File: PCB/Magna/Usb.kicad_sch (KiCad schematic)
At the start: 30 parts, among them J801 USB_A, J802 USB_C_Receptacle_USB2.0, J803 USB_B, U801 USBLC6-4SC6, U802 USB3300-EZK

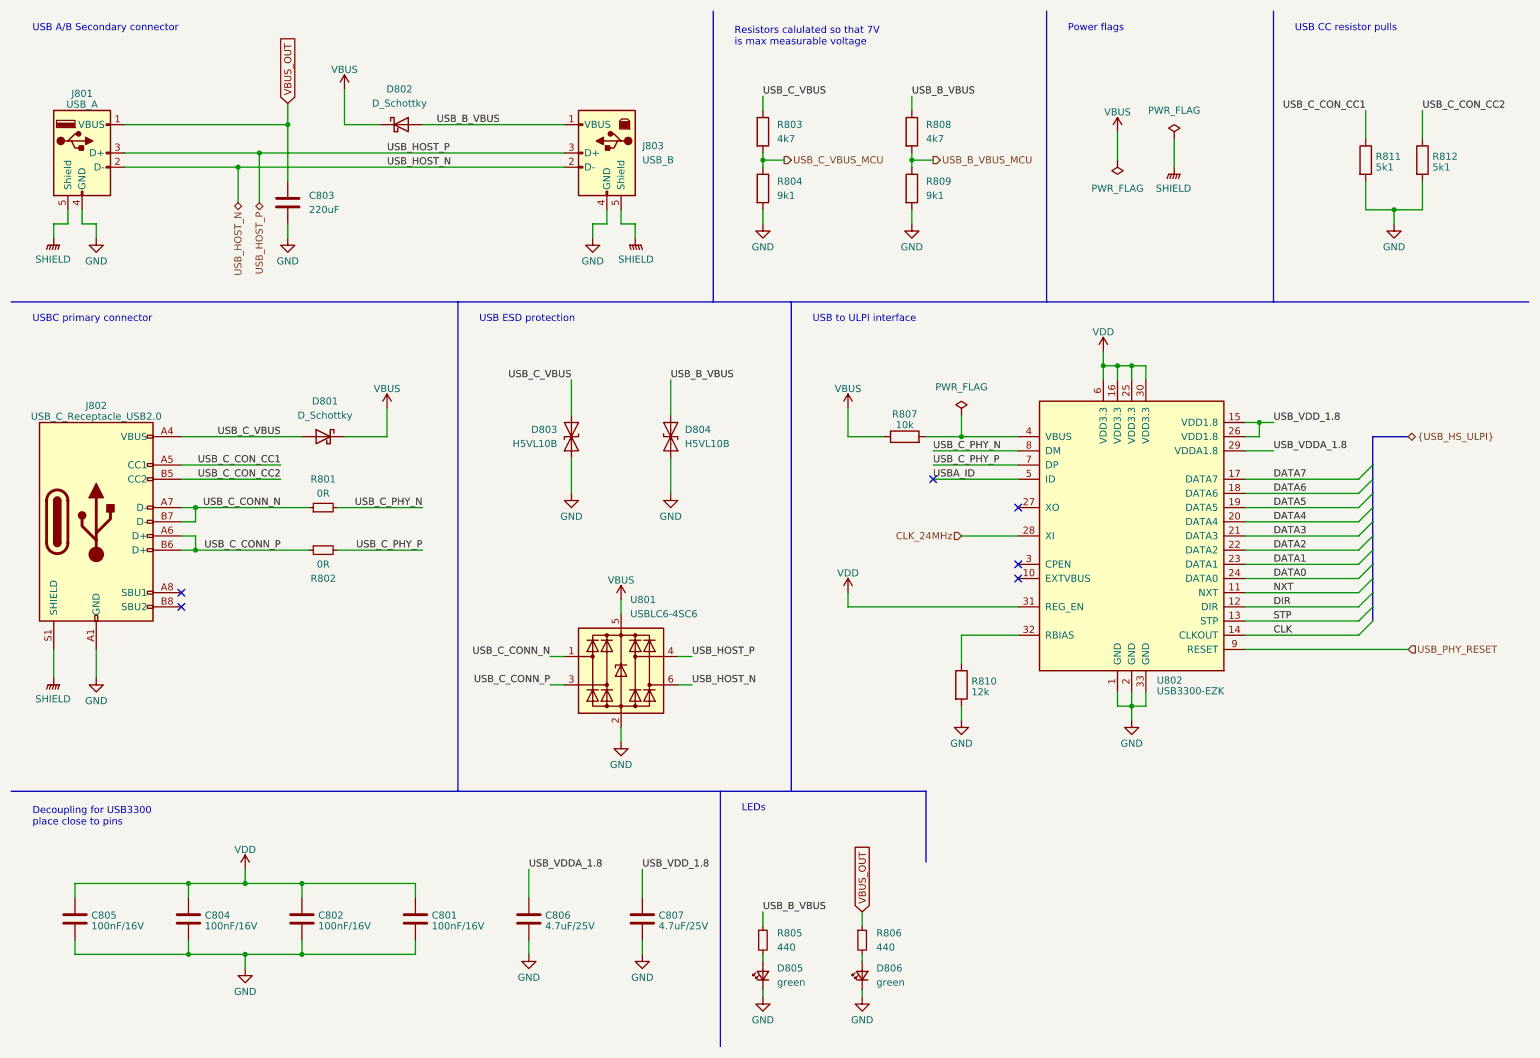
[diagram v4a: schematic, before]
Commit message: Select parts for all components
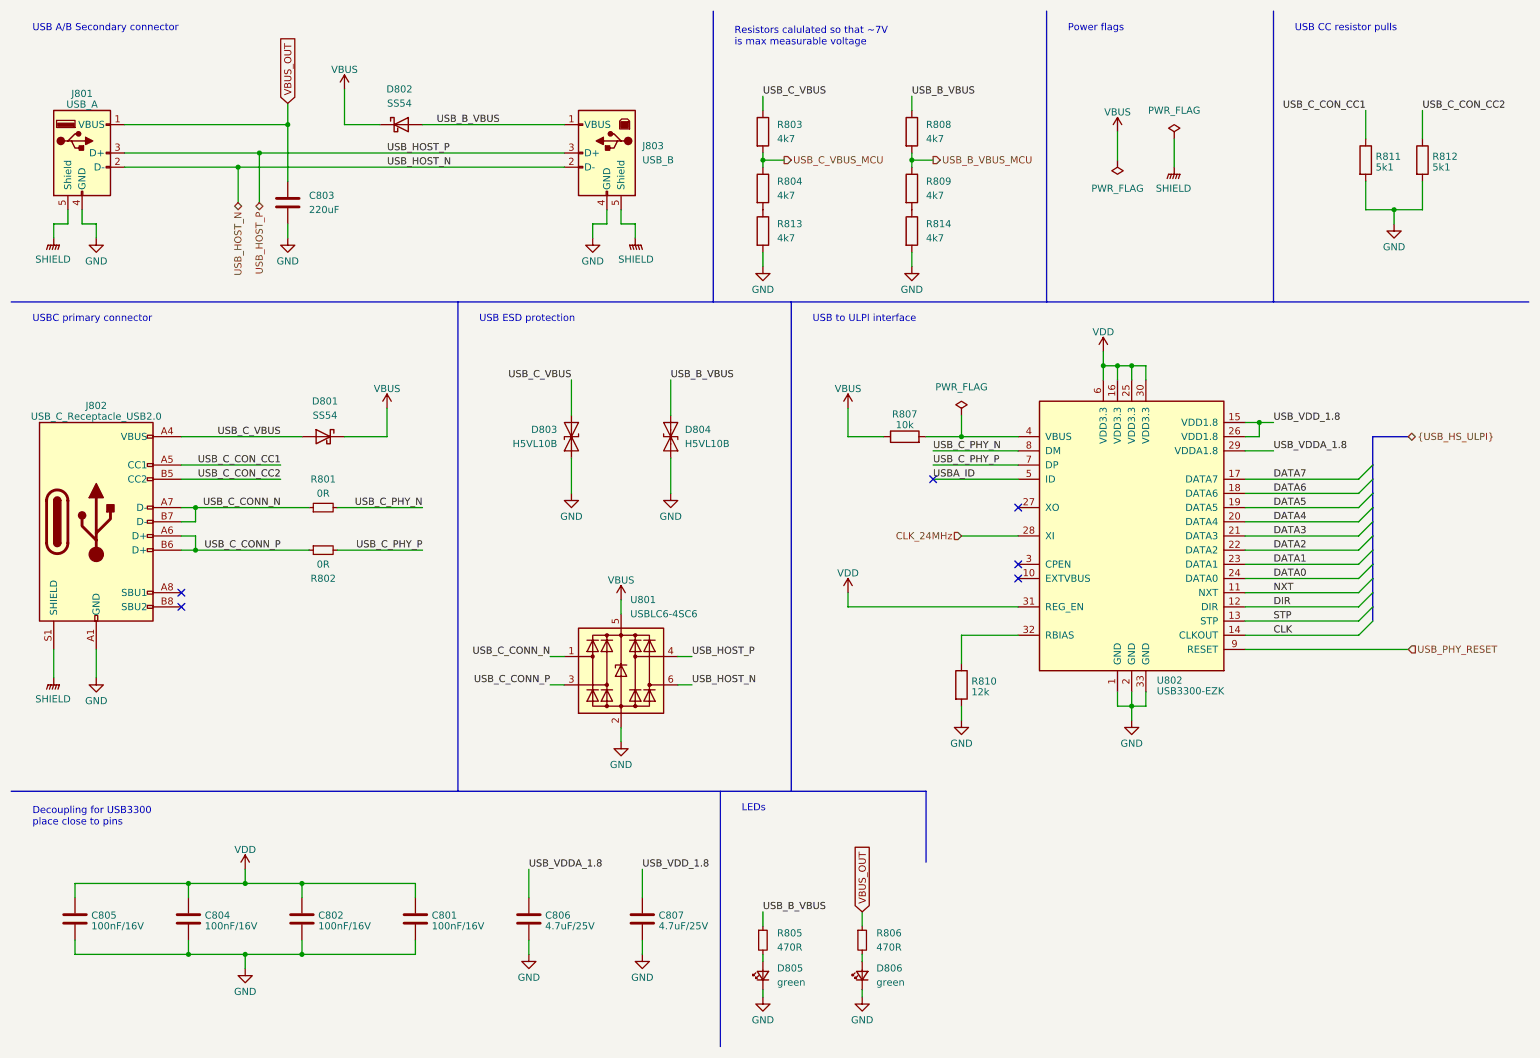
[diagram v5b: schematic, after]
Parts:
- added R813, R814: 4k7, Resistor_SMD:R_0805_2012Metric_Pad1.20x1.40mm_HandSolder, symbol Device:R
- D801, D802: value D_Schottky -> SS54; footprint (none) -> Diode_SMD:D_SMA_Handsoldering; LCSC (none) -> C22452
- D803, D804: LCSC (none) -> C7420372
- D805, D806: footprint (none) -> Diode_SMD:D_0805_2012Metric_Pad1.15x1.40mm_HandSolder; LCSC (none) -> C2297
- J801: footprint (none) -> Connector_USB:USB_A_Molex_67643_Horizontal; LCSC (none) -> C293351
- J802: footprint (none) -> Connector_USB:USB_C_Receptacle_G-Switch_GT-USB-7010ASV; LCSC (none) -> C2982555
- J803: footprint (none) -> Connector_USB:USB_B_OST_USB-B1HSxx_Horizontal; LCSC (none) -> C114097
- R801, R802: footprint (none) -> Resistor_SMD:R_0805_2012Metric; LCSC (none) -> C17477
- R803, R808: footprint (none) -> Resistor_SMD:R_0805_2012Metric_Pad1.20x1.40mm_HandSolder; LCSC (none) -> C17673
- R804, R809: value 9k1 -> 4k7; footprint (none) -> Resistor_SMD:R_0805_2012Metric_Pad1.20x1.40mm_HandSolder; LCSC (none) -> C17673
- R805, R806: value 440 -> 470R; footprint (none) -> Resistor_SMD:R_0805_2012Metric_Pad1.20x1.40mm_HandSolder; LCSC (none) -> C706320
- R807: footprint (none) -> Resistor_SMD:R_0805_2012Metric; LCSC (none) -> C17414
- R810: footprint (none) -> Resistor_SMD:R_0805_2012Metric_Pad1.20x1.40mm_HandSolder; LCSC (none) -> C17444
- U801: LCSC (none) -> C111212
- U802: LCSC (none) -> C108383
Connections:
- net GND: now also R813.2, R814.2; no longer R804.2, R809.2
- new net: R809.2, R814.1
- new net: R804.2, R813.1
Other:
- note added: "Resistors calulated so that ~7V is max measurable voltage"
- note removed: "Resistors calulated so that 7V is max measurable voltage"

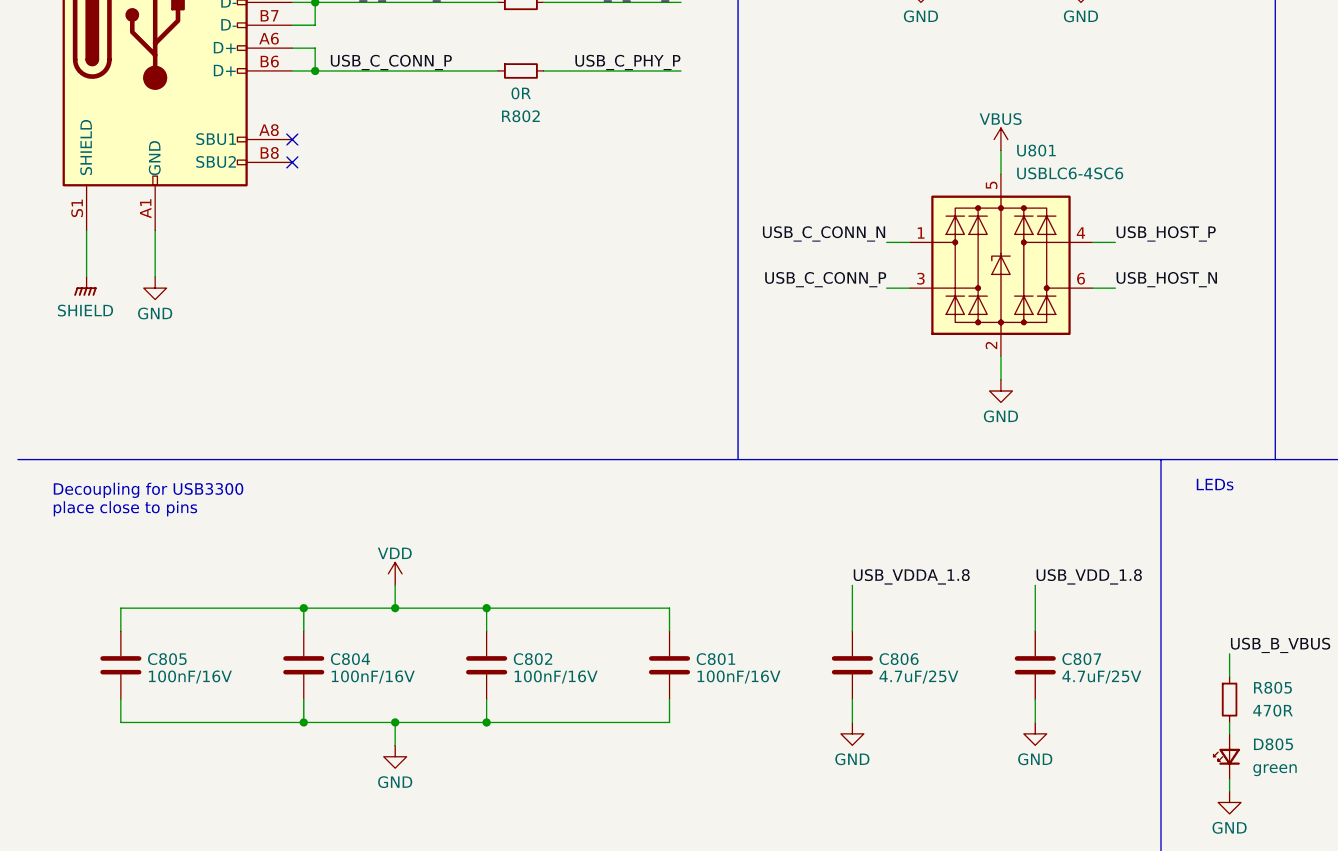
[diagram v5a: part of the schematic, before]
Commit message: Add even more component footprints and partnumbers
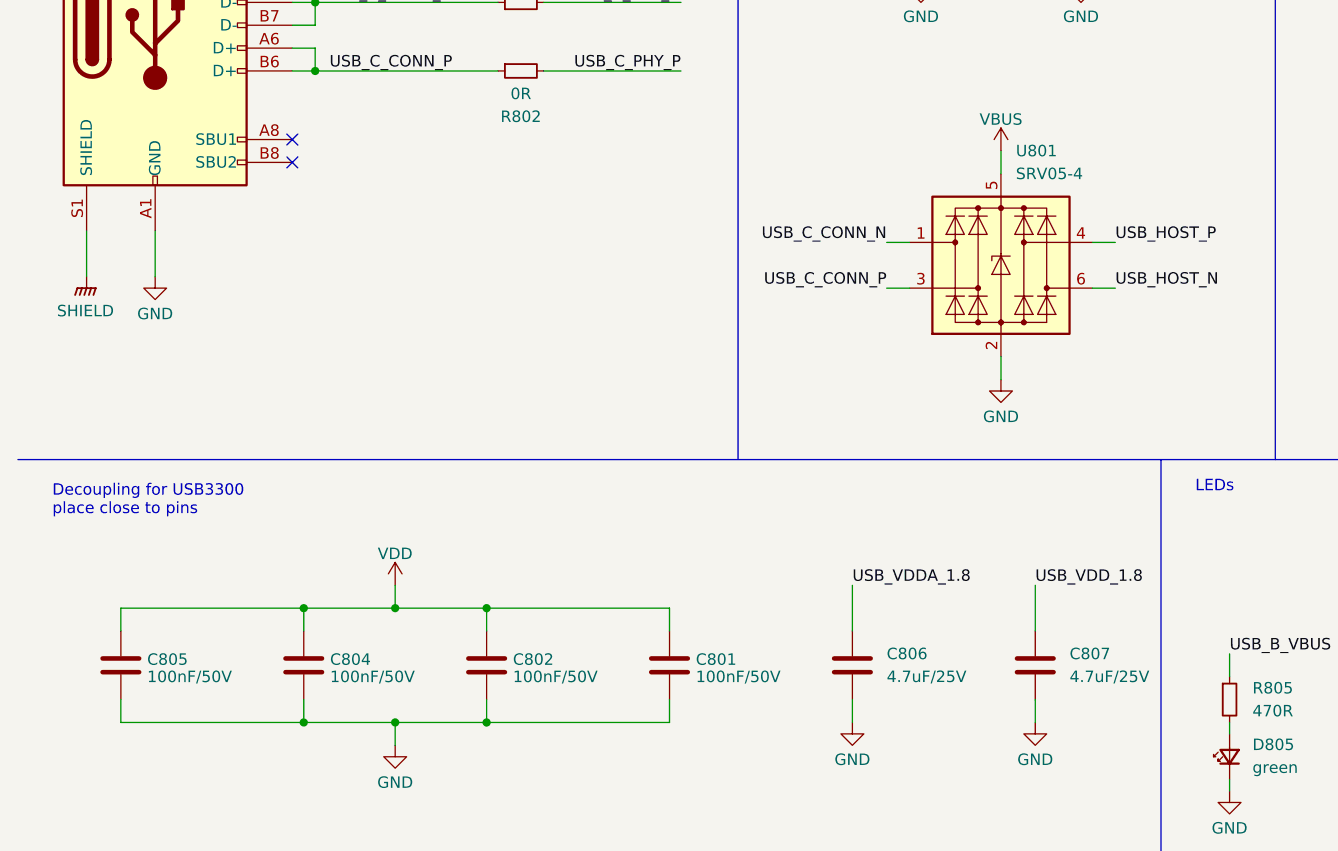
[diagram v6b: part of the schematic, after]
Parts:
- C801, C802, C804, C805: value 100nF/16V -> 100nF/50V; footprint Capacitor_SMD:C_0805_2012Metric -> Capacitor_SMD:C_0805_2012Metric_Pad1.18x1.45mm_HandSolder; LCSC C218638 -> C49678
- C806, C807: footprint Capacitor_SMD:C_0805_2012Metric -> Capacitor_SMD:C_0805_2012Metric_Pad1.18x1.45mm_HandSolder
- D803, D804: footprint (none) -> LED_SMD:LED_0402_1005Metric_Pad0.77x0.64mm_HandSolder
- R801, R802, R807, R811, R812: footprint Resistor_SMD:R_0805_2012Metric -> Resistor_SMD:R_0805_2012Metric_Pad1.20x1.40mm_HandSolder
- U801: value USBLC6-4SC6 -> SRV05-4; LCSC C111212 -> C7420376
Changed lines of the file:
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@@
       (effects (font (size 1.27 1.27)))
     )
-    (property "Footprint" "Resistor_SMD:R_0805_2012Metric" (at 172.72 90.678 90)
+    (property "Footprint" "Resistor_SMD:R_0805_2012Metric_Pad1.20x1.40mm_HandSolder" (at 172.72 90.678 90)
       (effects (font (size 1.27 1.27)) hide)
     )
@@
       (effects (font (size 1.27 1.27)) (justify left))
     )
-    (property "Footprint" "Resistor_SMD:R_0805_2012Metric" (at 263.652 39.37 90)
+    (property "Footprint" "Resistor_SMD:R_0805_2012Metric_Pad1.20x1.40mm_HandSolder" (at 263.652 39.37 90)
       (effects (font (size 1.27 1.27)) hide)
     )
@@
   (symbol (lib_id "Device:C") (at 125.73 175.26 0) (unit 1)
     (in_bom yes) (on_board yes) (dnp no) (fields_autoplaced)
-    (property "Reference" "C807" (at 128.651 174.6163 0)
-      (effects (font (size 1.27 1.27)) (justify left))
-    )
-    (property "Value" "4.7uF/25V" (at 128.651 176.5373 0)
-      (effects (font (size 1.27 1.27)) (justify left))
-    )
-    (property "Footprint" "Capacitor_SMD:C_0805_2012Metric" (at 126.6952 179.07 0)
+    (property "Reference" "C807" (at 129.54 173.99 0)
+      (effects (font (size 1.27 1.27)) (justify left))
+    )
+    (property "Value" "4.7uF/25V" (at 129.54 176.53 0)
+      (effects (font (size 1.27 1.27)) (justify left))
+    )
+    (property "Footprint" "Capacitor_SMD:C_0805_2012Metric_Pad1.18x1.45mm_HandSolder" (at 126.6952 179.07 0)
       (effects (font (size 1.27 1.27)) hide)
     )
@@
       (effects (font (size 1.27 1.27)))
     )
-    (property "Footprint" "Resistor_SMD:R_0805_2012Metric" (at 68.58 101.6 0)
+    (property "Footprint" "Resistor_SMD:R_0805_2012Metric_Pad1.20x1.40mm_HandSolder" (at 68.58 101.6 0)
       (effects (font (size 1.27 1.27)) hide)
     )
@@
       (effects (font (size 1.27 1.27)) (justify left))
     )
-    (property "Value" "100nF/16V" (at 67.691 176.5373 0)
-      (effects (font (size 1.27 1.27)) (justify left))
-    )
-    (property "Footprint" "Capacitor_SMD:C_0805_2012Metric" (at 65.7352 179.07 0)
+    (property "Value" "100nF/50V" (at 67.691 176.5373 0)
+      (effects (font (size 1.27 1.27)) (justify left))
+    )
+    (property "Footprint" "Capacitor_SMD:C_0805_2012Metric_Pad1.18x1.45mm_HandSolder" (at 65.7352 179.07 0)
       (effects (font (size 1.27 1.27)) hide)
     )
@@
       (effects (font (size 1.27 1.27)) hide)
     )
-    (property "LCSC" "C218638" (at 64.77 175.26 0)
+    (property "LCSC" "C49678" (at 64.77 175.26 0)
       (effects (font (size 1.27 1.27)) hide)
     )
@@
       (effects (font (size 1.27 1.27)) (justify right))
     )
-    (property "Footprint" "" (at 113.03 88.9 0)
+    (property "Footprint" "LED_SMD:LED_0402_1005Metric_Pad0.77x0.64mm_HandSolder" (at 113.03 88.9 0)
       (effects (font (size 1.27 1.27)) hide)
     )
@@
   (symbol (lib_id "Device:C") (at 105.41 175.26 0) (unit 1)
     (in_bom yes) (on_board yes) (dnp no) (fields_autoplaced)
-    (property "Reference" "C806" (at 108.331 174.6163 0)
-      (effects (font (size 1.27 1.27)) (justify left))
-    )
-    (property "Value" "4.7uF/25V" (at 108.331 176.5373 0)
-      (effects (font (size 1.27 1.27)) (justify left))
-    )
-    (property "Footprint" "Capacitor_SMD:C_0805_2012Metric" (at 106.3752 179.07 0)
+    (property "Reference" "C806" (at 109.22 173.99 0)
+      (effects (font (size 1.27 1.27)) (justify left))
+    )
+    (property "Value" "4.7uF/25V" (at 109.22 176.53 0)
+      (effects (font (size 1.27 1.27)) (justify left))
+    )
+    (property "Footprint" "Capacitor_SMD:C_0805_2012Metric_Pad1.18x1.45mm_HandSolder" (at 106.3752 179.07 0)
       (effects (font (size 1.27 1.27)) hide)
     )
@@
       (effects (font (size 1.27 1.27)))
     )
-    (property "Footprint" "Resistor_SMD:R_0805_2012Metric" (at 68.58 109.22 0)
+    (property "Footprint" "Resistor_SMD:R_0805_2012Metric_Pad1.20x1.40mm_HandSolder" (at 68.58 109.22 0)
       (effects (font (size 1.27 1.27)) hide)
     )
@@
       (effects (font (size 1.27 1.27)) (justify left))
     )
-    (property "Footprint" "Resistor_SMD:R_0805_2012Metric" (at 253.492 39.37 90)
+    (property "Footprint" "Resistor_SMD:R_0805_2012Metric_Pad1.20x1.40mm_HandSolder" (at 253.492 39.37 90)
       (effects (font (size 1.27 1.27)) hide)
     )
@@
       (effects (font (size 1.27 1.27)) (justify left))
     )
-    (property "Value" "100nF/16V" (at 47.371 176.5373 0)
-      (effects (font (size 1.27 1.27)) (justify left))
-    )
-    (property "Footprint" "Capacitor_SMD:C_0805_2012Metric" (at 45.4152 179.07 0)
+    (property "Value" "100nF/50V" (at 47.371 176.5373 0)
+      (effects (font (size 1.27 1.27)) (justify left))
+    )
+    (property "Footprint" "Capacitor_SMD:C_0805_2012Metric_Pad1.18x1.45mm_HandSolder" (at 45.4152 179.07 0)
       (effects (font (size 1.27 1.27)) hide)
     )
@@
       (effects (font (size 1.27 1.27)) hide)
     )
-    (property "LCSC" "C218638" (at 44.45 175.26 0)
+    (property "LCSC" "C49678" (at 44.45 175.26 0)
       (effects (font (size 1.27 1.27)) hide)
     )
@@
       (effects (font (size 1.27 1.27)) (justify left))
     )
-    (property "Value" "100nF/16V" (at 27.051 176.5373 0)
-      (effects (font (size 1.27 1.27)) (justify left))
-    )
-    (property "Footprint" "Capacitor_SMD:C_0805_2012Metric" (at 25.0952 179.07 0)
+    (property "Value" "100nF/50V" (at 27.051 176.5373 0)
+      (effects (font (size 1.27 1.27)) (justify left))
+    )
+    (property "Footprint" "Capacitor_SMD:C_0805_2012Metric_Pad1.18x1.45mm_HandSolder" (at 25.0952 179.07 0)
       (effects (font (size 1.27 1.27)) hide)
     )
@@
       (effects (font (size 1.27 1.27)) hide)
     )
-    (property "LCSC" "C218638" (at 24.13 175.26 0)
+    (property "LCSC" "C49678" (at 24.13 175.26 0)
       (effects (font (size 1.27 1.27)) hide)
     )
@@
       (effects (font (size 1.27 1.27)) (justify left))
     )
-    (property "Value" "100nF/16V" (at 88.011 176.5373 0)
-      (effects (font (size 1.27 1.27)) (justify left))
-    )
-    (property "Footprint" "Capacitor_SMD:C_0805_2012Metric" (at 86.0552 179.07 0)
+    (property "Value" "100nF/50V" (at 88.011 176.5373 0)
+      (effects (font (size 1.27 1.27)) (justify left))
+    )
+    (property "Footprint" "Capacitor_SMD:C_0805_2012Metric_Pad1.18x1.45mm_HandSolder" (at 86.0552 179.07 0)
       (effects (font (size 1.27 1.27)) hide)
     )
@@
       (effects (font (size 1.27 1.27)) hide)
     )
-    (property "LCSC" "C218638" (at 85.09 175.26 0)
+    (property "LCSC" "C49678" (at 85.09 175.26 0)
       (effects (font (size 1.27 1.27)) hide)
     )
@@
       (effects (font (size 1.27 1.27)) (justify right))
     )
-    (property "Footprint" "" (at 130.81 88.9 0)
+    (property "Footprint" "LED_SMD:LED_0402_1005Metric_Pad0.77x0.64mm_HandSolder" (at 130.81 88.9 0)
       (effects (font (size 1.27 1.27)) hide)
     )
@@
       (effects (font (size 1.27 1.27)) (justify left))
     )
-    (property "Value" "USBLC6-4SC6" (at 123.5711 120.65 0)
+    (property "Value" "SRV05-4" (at 123.5711 120.65 0)
       (effects (font (size 1.27 1.27)) (justify left))
     )
@@
       (effects (font (size 1.27 1.27)) hide)
     )
-    (property "Datasheet" "https://www.st.com/resource/en/datasheet/usblc6-4.pdf" (at 127 121.92 0)
-      (effects (font (size 1.27 1.27)) hide)
-    )
-    (property "LCSC" "C111212" (at 121.92 130.81 0)
-      (effects (font (size 1.27 1.27)) hide)
-    )
+    (property "Datasheet" "https://datasheet.lcsc.com/lcsc/2308281515_hongjiacheng-SRV05-4_C7420376.pdf" (at 127 121.92 0)
+      (effects (font (size 1.27 1.27)) hide)
+    )
+    (property "LCSC" "C7420376" (at 121.92 130.81 0)
+      (effects (font (size 1.27 1.27)) hide)
+    )
